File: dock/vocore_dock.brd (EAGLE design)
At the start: 25.6 x 25.6 mm, 34 parts

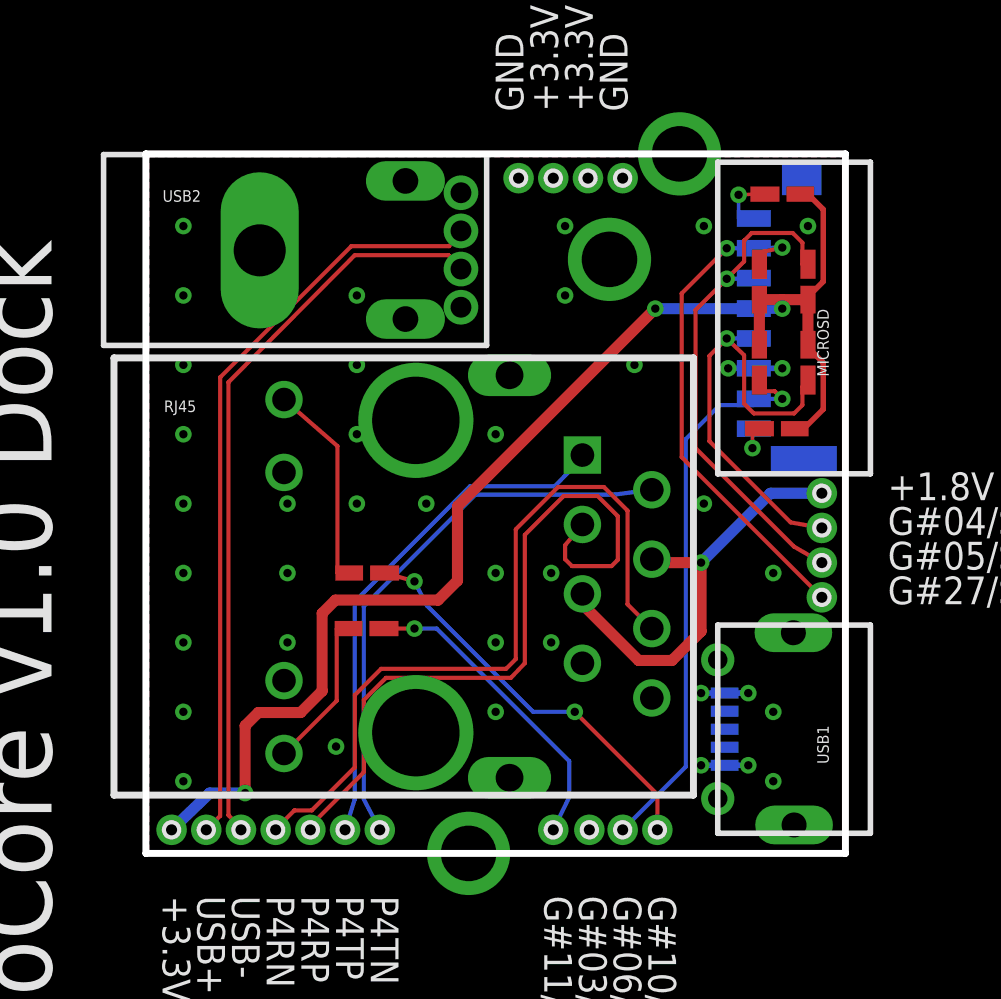
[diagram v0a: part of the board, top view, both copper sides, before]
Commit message: created schematic schematic/brd are in sync. gnd's are missing. some holes wrong size. DRC is wrong restrings?
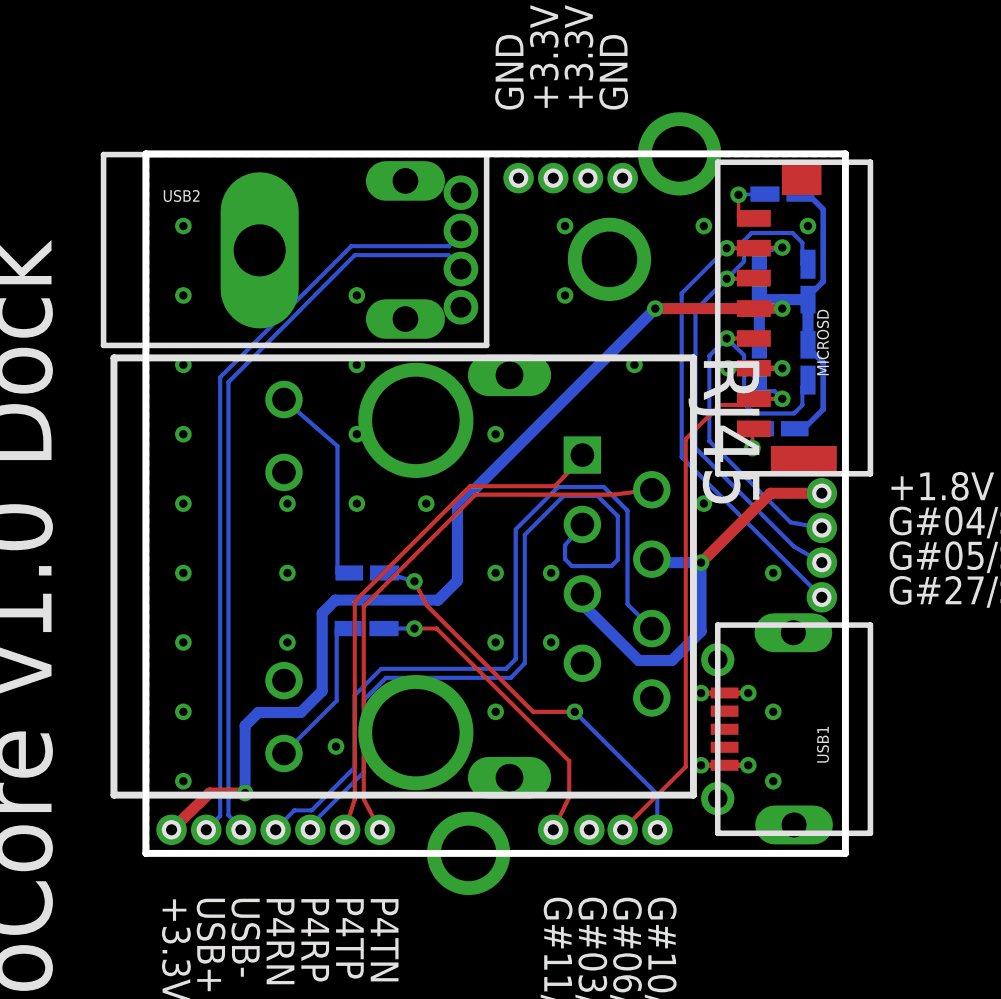
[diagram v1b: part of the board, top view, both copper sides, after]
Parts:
- PB04, PB05, PB06, PB07, PB12, PB13, PB14, PB15, PB16, PB17, PB18, PL05, PL06, PL07, PL08, PT01, PT02, PT03, PT04: value PORT_1PIN_DECAL -> PORT_1PIN; device VoCore.dock.pcb:PORT_1PIN_DECAL_1PRIMARY -> vocore_dock:PORT_1PIN_DECAL_1PRIMARY

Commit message: adding gnd's
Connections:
- net GND: now also MICROSD.10, MICROSD.9, RJ45.8
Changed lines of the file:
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@@
 <vertex x="246.38" y="236.22"/>
 </polygon>
+<contactref element="RJ45" pad="8"/>
+<contactref element="MICROSD" pad="10"/>
+<contactref element="MICROSD" pad="9"/>
 </signal>
 <signal name="SPI_CLK">
